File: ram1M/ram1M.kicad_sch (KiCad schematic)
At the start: 4 parts, among them J1 ramslot, U1 74HC32, U2 AS6C4008-55PCN, U3 AS6C4008-55PCN

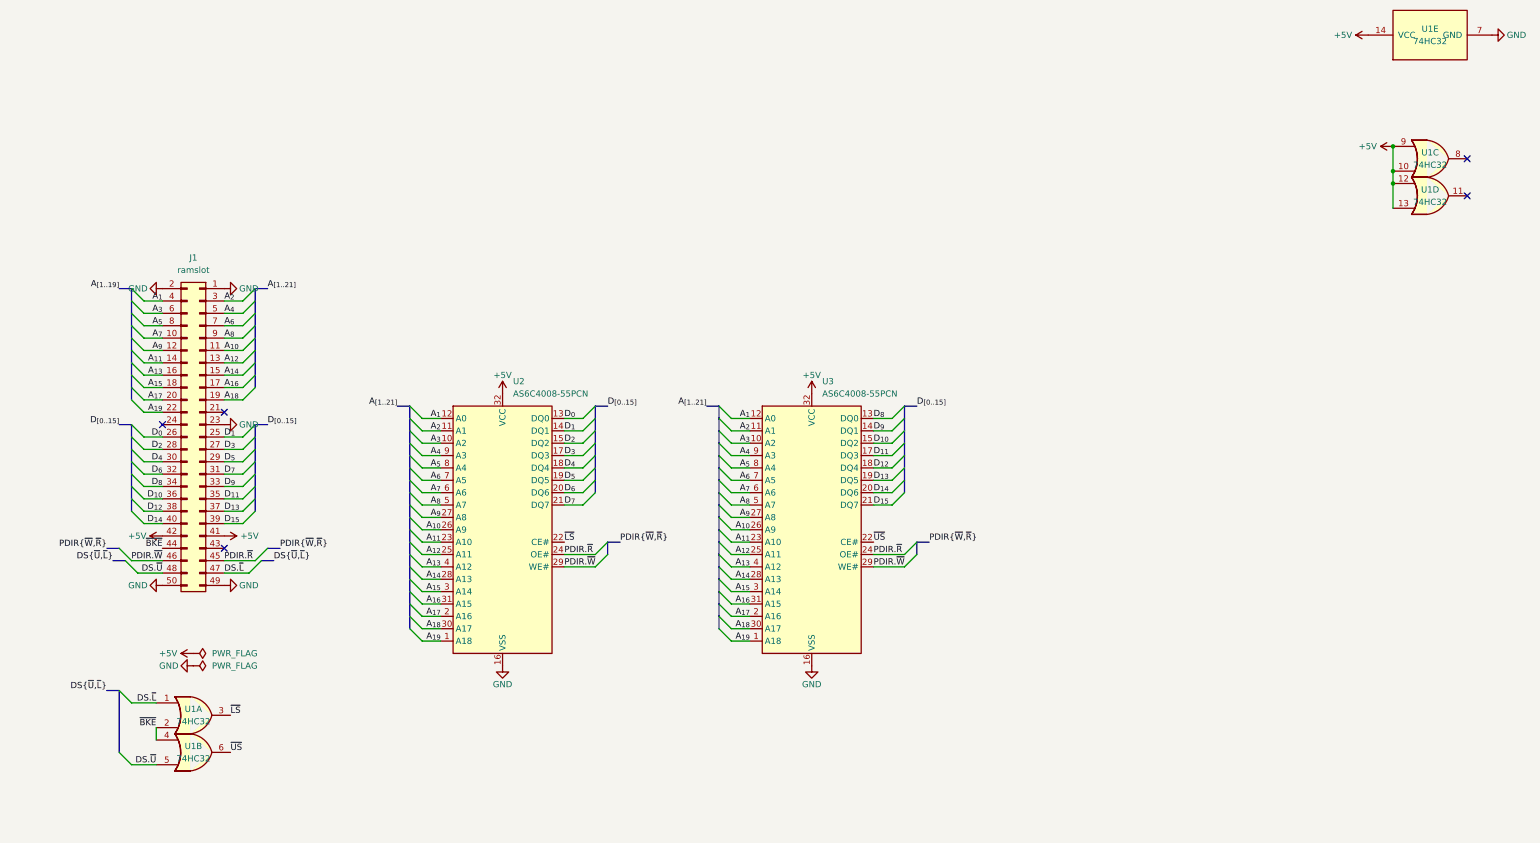
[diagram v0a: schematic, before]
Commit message: [ram1M] restored from a SF68 backup
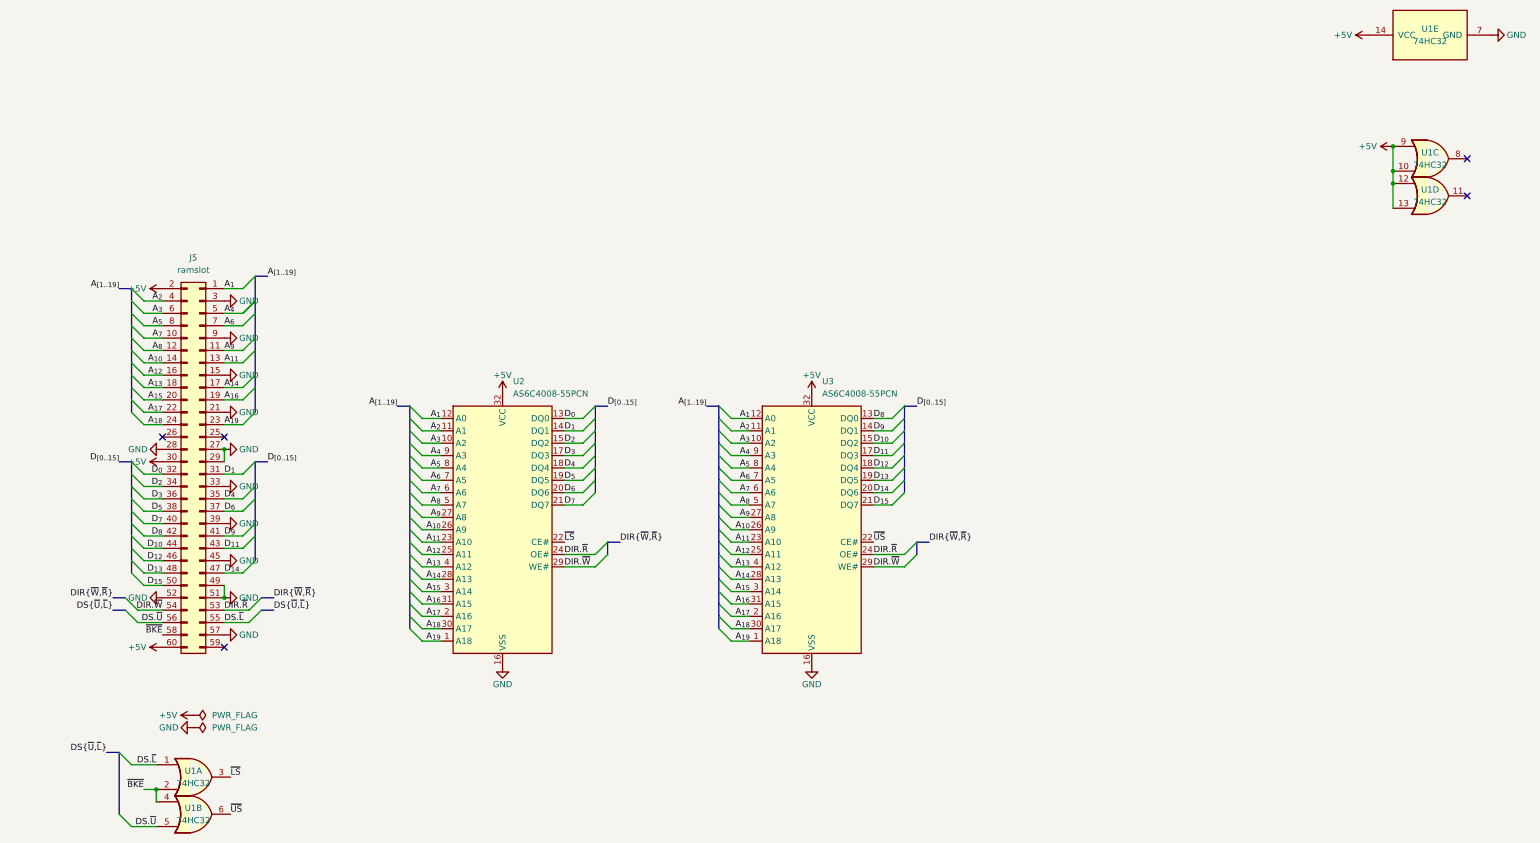
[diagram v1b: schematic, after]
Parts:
- removed J1: ramslot, Connector_PCBEdge:pcb_edge_50_P2.54, symbol Connector_Generic:Conn_02x25_Odd_Even
- added J5: ramslot, Connector_PCBEdge:pcb_edge_60_P2.54_new, symbol Connector_Generic:Conn_02x30_Odd_Even
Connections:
- net +5V: now also J5.2 (Pin_2), J5.30 (Pin_30), J5.60 (Pin_60)
- net A_{10}: now also J5.14 (Pin_14)
- net A_{11}: now also J5.13 (Pin_13)
- net A_{12}: now also J5.16 (Pin_16)
- net A_{13}: now also J5.18 (Pin_18)
- net A_{14}: now also J5.17 (Pin_17)
- net A_{15}: now also J5.20 (Pin_20)
- net A_{16}: now also J5.19 (Pin_19)
- net A_{17}: now also J5.22 (Pin_22)
- net A_{18}: now also J5.24 (Pin_24)
- net A_{19}: now also J5.23 (Pin_23)
- net A_{1}: now also J5.1 (Pin_1)
- net A_{2}: now also J5.4 (Pin_4)
- net A_{3}: now also J5.6 (Pin_6)
- net A_{4}: now also J5.5 (Pin_5)
- net A_{5}: now also J5.8 (Pin_8)
- net A_{6}: now also J5.7 (Pin_7)
- net A_{7}: now also J5.10 (Pin_10)
- net A_{8}: now also J5.12 (Pin_12)
- net A_{9}: now also J5.11 (Pin_11)
- net DS.~{L}: now also J5.55 (Pin_55)
- net DS.~{U}: now also J5.56 (Pin_56)
- net D_{0}: now also J5.32 (Pin_32)
- net D_{10}: now also J5.44 (Pin_44)
- net D_{11}: now also J5.43 (Pin_43)
- net D_{12}: now also J5.46 (Pin_46)
- net D_{13}: now also J5.48 (Pin_48)
- net D_{14}: now also J5.47 (Pin_47)
- net D_{15}: now also J5.50 (Pin_50)
- net D_{1}: now also J5.31 (Pin_31)
- net D_{2}: now also J5.34 (Pin_34)
- net D_{3}: now also J5.36 (Pin_36)
- net D_{4}: now also J5.35 (Pin_35)
- net D_{5}: now also J5.38 (Pin_38)
- net D_{6}: now also J5.37 (Pin_37)
- net D_{7}: now also J5.40 (Pin_40)
- net D_{8}: now also J5.42 (Pin_42)
- net D_{9}: now also J5.41 (Pin_41)
- net GND: now also J5.15 (Pin_15), J5.21 (Pin_21), J5.27 (Pin_27), J5.28 (Pin_28), J5.29 (Pin_29), J5.3 (Pin_3), J5.33 (Pin_33), J5.39 (Pin_39), J5.45 (Pin_45), J5.49 (Pin_49), J5.51 (Pin_51), J5.52 (Pin_52), J5.57 (Pin_57), J5.9 (Pin_9)
- net ~{BKE}: now also J5.58 (Pin_58)
- net PDIR.~{R} renamed DIR.~{R}
- net DIR.~{R}: now also J5.53 (Pin_53)
- net PDIR.~{W} renamed DIR.~{W}
- net DIR.~{W}: now also J5.54 (Pin_54)
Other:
- moved on the sheet: U1A, U1B
